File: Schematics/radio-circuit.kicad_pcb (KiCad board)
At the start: 4 copper layers, 58.8 x 29.5 mm, 36 parts, among them J1 USB_B_Micro, J2 STDC14, J3 0, U1 USBLC6-2SC6, U2 LD39015M33R, U3 STM32F042C6T6, U4 Si4705-D60-GM, Y1 SG-3030CM

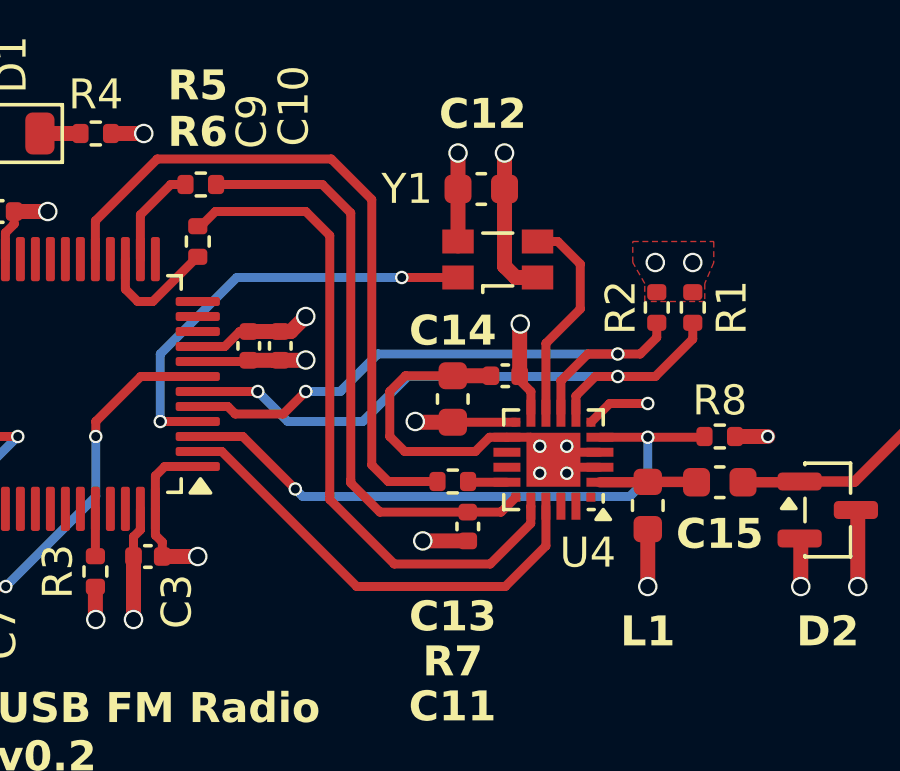
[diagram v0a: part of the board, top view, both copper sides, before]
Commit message: Took the new footprint into use
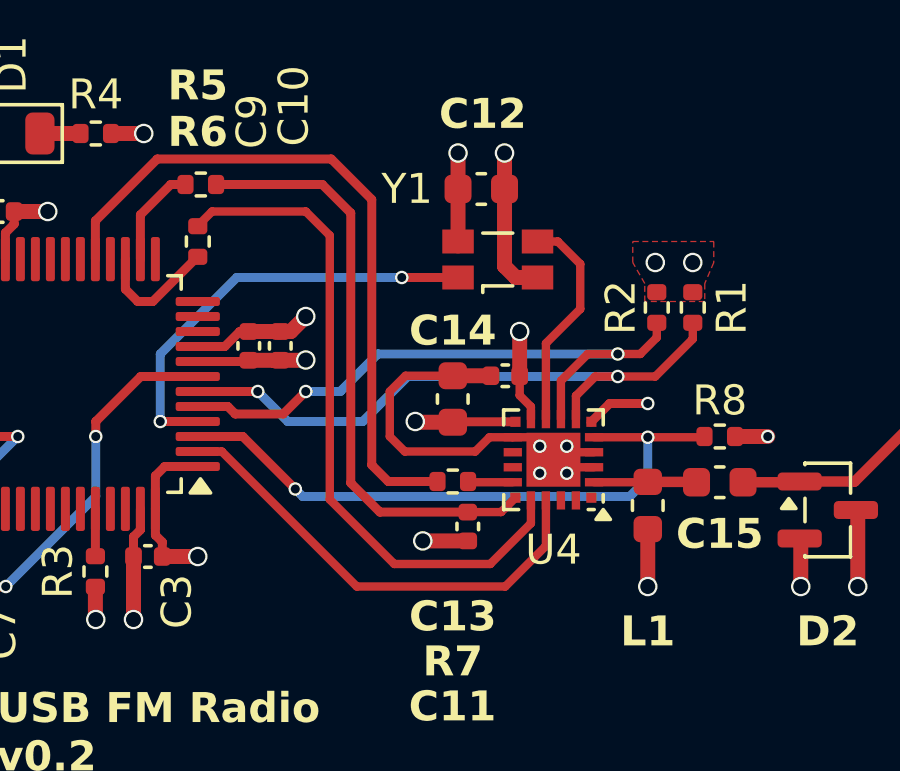
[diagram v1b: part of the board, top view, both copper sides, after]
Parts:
- J3: footprint Connector_Coaxial:SMA_BAT_Wireless_BWSMA-KWE-Z001 -> Local:SMA_BAT_Wireless_BWSMA-KE-Z001
- U4: footprint Package_DFN_QFN:SiliconLabs_QFN-20-1EP_3x3mm_P0.5mm_EP1.8x1.8mm -> Local:Skyworks_QFN-20-1EP_3x3mm_P0.5mm_EP1.8x1.8mm

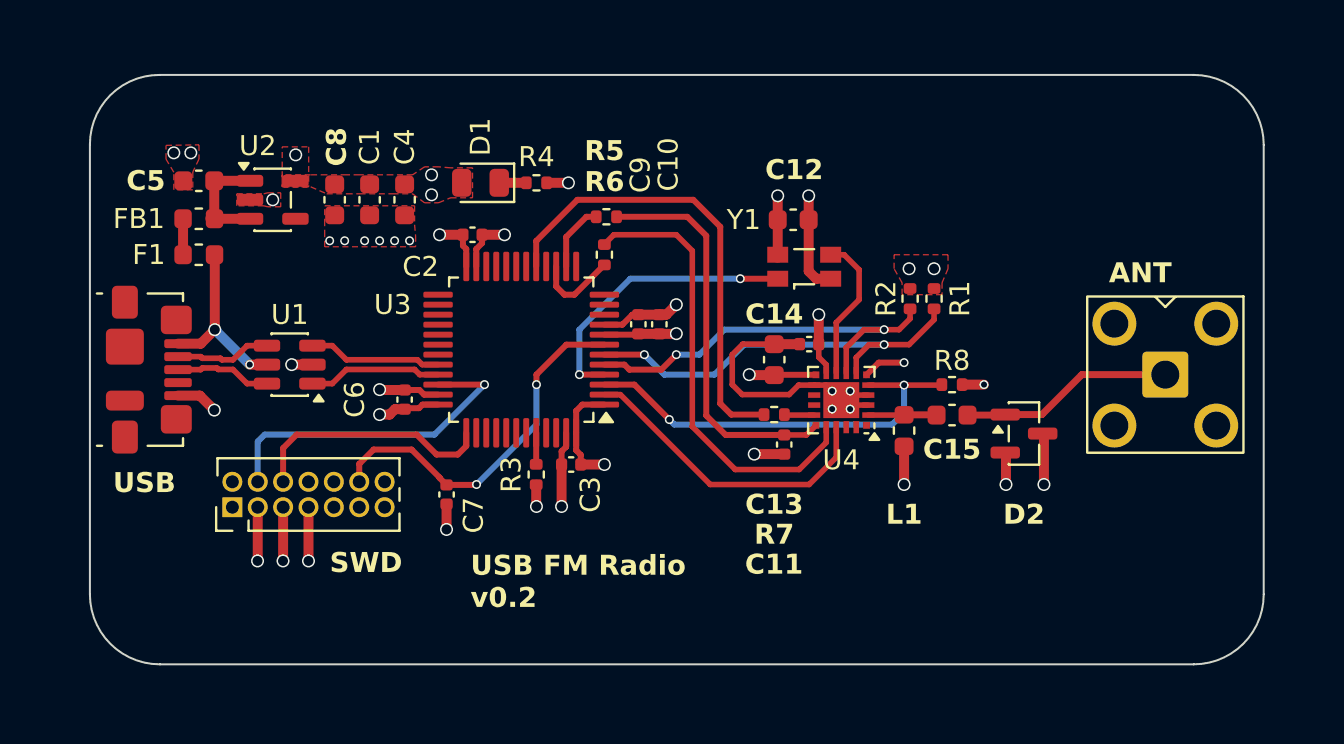
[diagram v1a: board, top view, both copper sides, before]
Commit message: New PCB version with STM32F042F6Px
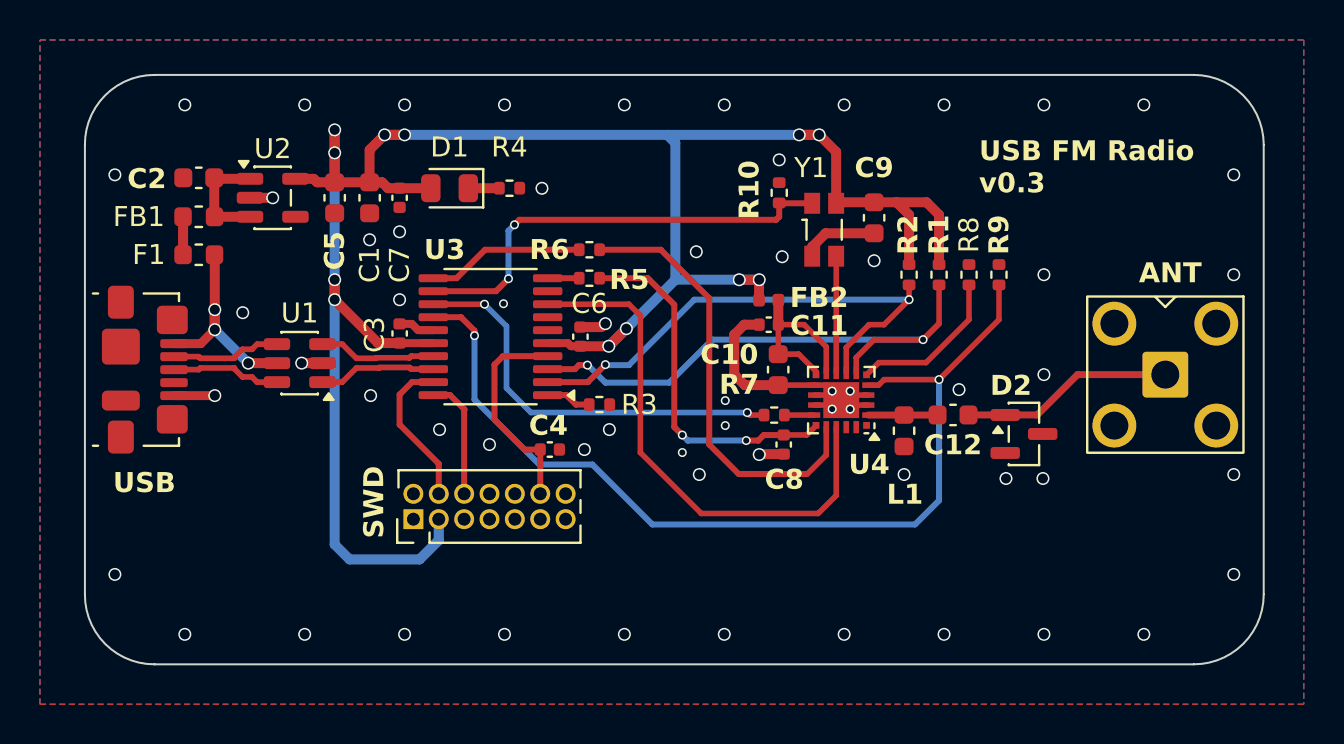
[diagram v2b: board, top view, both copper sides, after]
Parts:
- removed C13: 22n, Capacitor_SMD:C_0603_1608Metric
- removed C14: 100n, Capacitor_SMD:C_0402_1005Metric
- removed C15: 1n, Capacitor_SMD:C_0603_1608Metric
- added FB2: 600@100MHz, Inductor_SMD:L_0402_1005Metric, F.Cu at (196.2, 121.3)
- added R10: 10k, Resistor_SMD:R_0402_1005Metric, F.Cu at (196.8, 115.9)
- added R9: 10k, Resistor_SMD:R_0402_1005Metric, F.Cu at (207.8, 120.0)
- C10: value 1u -> 22n; footprint Capacitor_SMD:C_0402_1005Metric -> Capacitor_SMD:C_0603_1608Metric
- C11: value 2.2p -> 100n
- C12: value 47n -> 1n
- C2: value 100n -> 4.7u; footprint Capacitor_SMD:C_0402_1005Metric -> Capacitor_SMD:C_0603_1608Metric
- C4: value 4.7u -> 100n; footprint Capacitor_SMD:C_0603_1608Metric -> Capacitor_SMD:C_0402_1005Metric
- C6: value 100n -> 10n
- C7: value 100n -> 1u
- C8: value 4.7u -> 2.2p; footprint Capacitor_SMD:C_0603_1608Metric -> Capacitor_SMD:C_0402_1005Metric
- C9: value 10n -> 47n; footprint Capacitor_SMD:C_0402_1005Metric -> Capacitor_SMD:C_0603_1608Metric
- U3: value STM32F042C6T6 -> STM32F042F6Px; footprint Package_QFP:LQFP-48_7x7mm_P0.5mm -> Package_SO:TSSOP-20_4.4x6.5mm_P0.65mm
- moved C8 25.6 mm to (197.0, 128.5)
- moved C7 15.0 mm to (177.8, 116.2)
- moved C4 14.5 mm to (185.3, 128.8), turned to 0 degrees
- moved C2 14.0 mm to (167.7, 115.2), turned to 180 degrees
- moved C9 12.9 mm to (201.5, 117.2)
- moved C12 12.6 mm to (205.4, 127.0), turned to 180 degrees
- moved C3 10.8 mm to (177.8, 122.9), turned to 90 degrees
- moved C6 9.35 mm to (186.8, 123.1)
- moved J2 9.08 mm to (178.4, 132.2)
- moved C5 6.85 mm to (174.5, 116.2), turned to -90 degrees
- moved C10 6.37 mm to (196.7, 124.8)
- moved C11 6.05 mm to (196.2, 122.5), turned to 180 degrees
- moved R8 5.57 mm to (206.2, 120.0), turned to -90 degrees
- moved R3 4.72 mm to (187.8, 126.5), turned to 0 degrees
- moved R5 3.19 mm to (187.2, 120.2)
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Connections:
- net VBUS renamed V_{BUS}
- C10 pad 1: +3.3V -> V_{A}
- C11 pad 1: I2S_WS -> V_{A}
- C12 pad 1: +3.3V -> /ANT
- C12 pad 2: GND -> /FMI
- C2 pad 1: +3.3V -> V_{FILT}
- C4 pad 1: +3.3V -> NRST
- C5 pad 1: /LD_IN -> +3.3V
- C7 pad 1: NRST -> +3.3V
- C8 pad 1: +3.3V -> I2S_WS
- FB1 pad 2: /LD_IN -> V_{FILT}
- R8 pad 2: ~{RST} -> / ~{SEN}
- U2 pad 1: /LD_IN -> V_{FILT}
- U2 pad 3: /LD_IN -> V_{FILT}
- U3 pad 1: +3.3V -> /BOOT
- U3 pad 10: unconnected-(U3-PA0-Pad10) -> /PA4
- U3 pad 11: unconnected-(U3-PA1-Pad11) -> /PA5
- U3 pad 12: unconnected-(U3-PA2-Pad12) -> OSC_EN
- U3 pad 13: unconnected-(U3-PA3-Pad13) -> I2S_SD
- U3 pad 14: /PA4 -> ~{RD_RST}
- U3 pad 15: /PA5 -> GND
- U3 pad 16: unconnected-(U3-PA6-Pad16) -> +3.3V
- U3 pad 17: I2S_SD -> USB_D-
- U3 pad 18: unconnected-(U3-PB0-Pad18) -> USB_D+
- U3 pad 19: unconnected-(U3-PB1-Pad19) -> SWDIO
- U3 pad 2: ~{INT} -> I2C_SDA
- U3 pad 20: unconnected-(U3-PB2-Pad20) -> SWCLK
- U3 pad 3: ~{RST} -> I2C_SCL
- U3 pad 4: RCLK_EN -> NRST
- U3 pad 5: I2C_SDA -> +3.3V
- U3 pad 6: I2C_SCL -> unconnected-(U3-PA0-Pad6)
- U3 pad 7: NRST -> unconnected-(U3-PA1-Pad7)
- U3 pad 8: GND -> ~{RD_IRQ}
- U3 pad 9: +3.3V -> unconnected-(U3-PA3-Pad9)
- U4 pad 10: +3.3V -> V_{A}
- U4 pad 11: +3.3V -> V_{A}
- U4 pad 13: unconnected-(U4-ROUT/[DOUT]-Pad13) -> GND
- U4 pad 14: unconnected-(U4-LOUT[DFS]-Pad14) -> GND
- U4 pad 18: ~{INT} -> ~{RD_IRQ}
- U4 pad 5: ~{RST} -> ~{RD_RST}
- U4 pad 6: GND -> / ~{SEN}
- Y1 pad 1: RCLK_EN -> OSC_EN
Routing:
- net +3.3V: track 27.5 -> 108.3 mm, vias 13 -> 12
- net ~{RD_RST}: track 0.00 -> 47.8 mm, vias 0 -> 2
- net GND: track 53.3 -> 24.3 mm, vias 31 -> 60
- net ~{RD_IRQ}: track 0.00 -> 26.6 mm
- net OSC_EN: track 0.00 -> 22.6 mm, vias 0 -> 2
- net ~{RST}: track 21.2 -> 0.00 mm, vias 2 -> 0
- net ~{INT}: track 15.5 -> 0.00 mm
- net RCLK_EN: track 14.5 -> 0.00 mm, vias 2 -> 0
- net V_{A}: track 0.00 -> 9.48 mm
- net SWDIO: track 16.9 -> 7.72 mm, vias 1 -> 0
- net / ~{SEN}: track 0.00 -> 8.03 mm
- net NRST: track 18.6 -> 10.7 mm, vias 2 -> 0
- net I2C_SCL: track 21.0 -> 27.7 mm
- net SWCLK: track 12.4 -> 6.09 mm
- net I2C_SDA: track 20.5 -> 26.0 mm
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- added copper zone on B.Cu, net GND
- added copper zone on In2.Cu, net GND
- removed copper zone on F.Cu, net +3.3V
- removed copper zone on In2.Cu, net +3.3V
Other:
- board size 58.8 x 29.5 mm -> 59 x 29.5 mm
- board text added: "USB FM Radio v0.3"
- board text removed: "USB FM Radio v0.2"

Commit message: Took connector into use, and started a new PCB layout
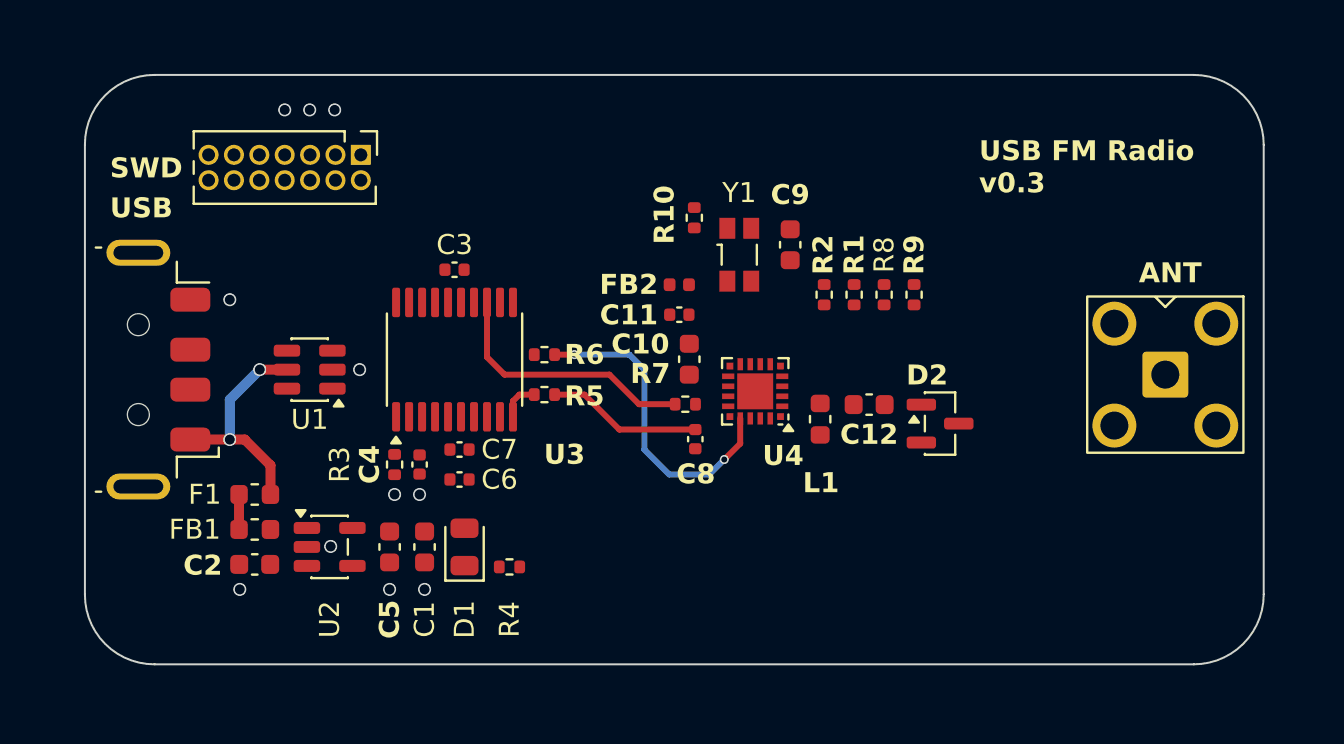
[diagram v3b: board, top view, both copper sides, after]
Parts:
- removed J1: USB_B_Micro, Connector_USB:USB_Micro-B_Molex_47346-0001
- added J4: USB_A, Local:USB_A_Molex_48037-2200_Horizontal, F.Cu at (156.3, 124.8)
- moved C2 19.6 mm to (170.5, 134.5)
- moved R4 19.0 mm to (183.2, 134.6)
- moved J2 18.4 mm to (175.8, 114.0), turned to -90 degrees
- moved D1 18.0 mm to (181.0, 133.6), turned to 90 degrees
- moved U2 17.7 mm to (174.2, 133.6)
- moved C1 17.7 mm to (179.0, 133.6)
- moved C5 17.7 mm to (177.2, 133.6)
- moved FB1 15.9 mm to (170.5, 132.8)
- moved C7 13.0 mm to (180.8, 128.8), turned to 0 degrees
- moved F1 12.3 mm to (170.5, 131.0)
- moved R3 10.7 mm to (177.5, 129.5), turned to -90 degrees
- moved C6 9.37 mm to (180.8, 130.2), turned to 0 degrees
- moved C4 6.56 mm to (178.8, 129.5), turned to -90 degrees
- moved R5 6.24 mm to (185.0, 126.0)
- moved R6 5.71 mm to (185.0, 124.0)
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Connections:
- net V_{A} renamed V_{RADIO}
- U1 pad 1: USB_D+ -> USB_D-
- U1 pad 3: USB_D- -> USB_D+
- U1 pad 4: /USB_CONN_D- -> /USB_CONN_D+
- U1 pad 6: /USB_CONN_D+ -> /USB_CONN_D-
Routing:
- net +3.3V: track 108.3 -> 0.00 mm, vias 12 -> 1
- net ~{RD_RST}: track 47.8 -> 0.00 mm, vias 2 -> 0
- net I2C_SCL: track 27.7 -> 0.00 mm, vias 2 -> 0
- net ~{RD_IRQ}: track 26.6 -> 0.00 mm
- net I2C_SDA: track 26.0 -> 0.00 mm, vias 2 -> 0
- net GND: track 24.3 -> 0.00 mm, vias 60 -> 10
- net OSC_EN: track 22.6 -> 0.00 mm, vias 2 -> 0
- net NRST: track 10.7 -> 0.00 mm
- net /ANT: track 10.7 -> 0.00 mm
- net I2S_WS: track 18.1 -> 7.76 mm, vias 2 -> 0
- net V_{RADIO}: track 9.48 -> 0.00 mm
- net / ~{SEN}: track 8.03 -> 0.00 mm
- net /PA5: track 7.89 -> 0.00 mm
- net SWDIO: track 7.72 -> 0.00 mm
- net I2S_SD: track 20.7 -> 13.1 mm, vias 2 -> 0
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- removed copper zone on B.Cu, net GND
- removed copper zone on F.Cu, net GND
- removed copper zone on In1.Cu, net GND
- removed copper zone on In2.Cu, net GND
